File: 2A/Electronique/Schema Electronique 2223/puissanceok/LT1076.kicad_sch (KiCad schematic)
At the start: 10 parts

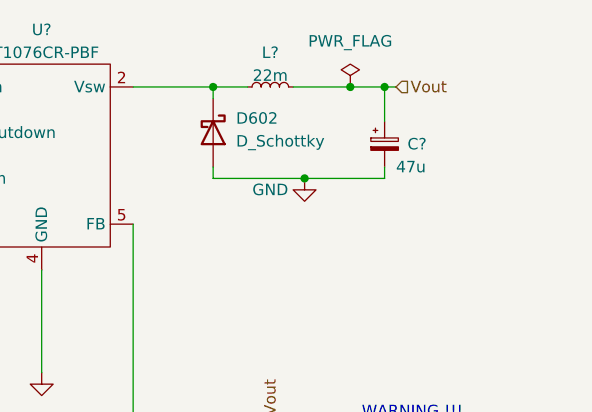
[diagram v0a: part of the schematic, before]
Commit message: pcb place components and add power/gnd planes
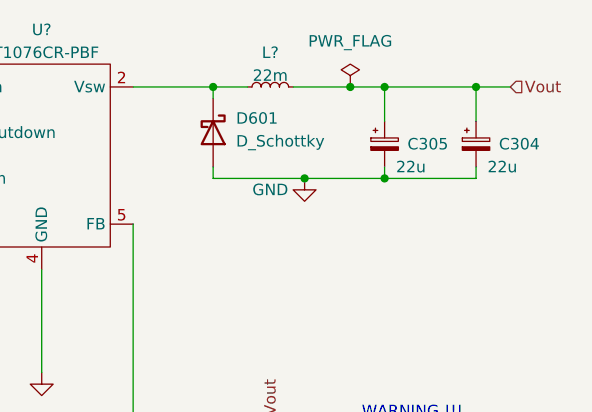
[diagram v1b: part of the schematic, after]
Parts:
- removed C?: 47u, Capacitor_SMD:CP_Elec_6.3x5.4, symbol Device:C_Polarized_Small
- added C304, C305: 22u, Capacitor_SMD:CP_Elec_4x5.4, symbol Device:C_Polarized_Small
- renumbered D602 to D601
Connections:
- net GND: now also C304.2, C305.2
- net Vout: now also C304.1, C305.1

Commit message: update pcb
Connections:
- net voutbuck: now reaches D601.1 (K), L?.1, U?.2 (Vsw)
- net vc: now reaches R?.1, U?.6 (Vc)
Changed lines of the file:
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@@
+    (effects (font (size 1.27 1.27)) (justify left bottom))
+  )
+  (label "voutbuck" (at 135.382 68.58 0) (fields_autoplaced)
+    (effects (font (size 1.27 1.27)) (justify left bottom))
+  )
+  (label "vc" (at 110.744 83.82 0) (fields_autoplaced)
     (effects (font (size 1.27 1.27)) (justify left bottom))
   )
